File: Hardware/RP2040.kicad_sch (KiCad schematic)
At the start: 29 parts, among them J1 USB_B, SW2 SW_Push_Dual, U1 W25Q128JVS, U2 RP2040, Y1 ABM8-272-T3

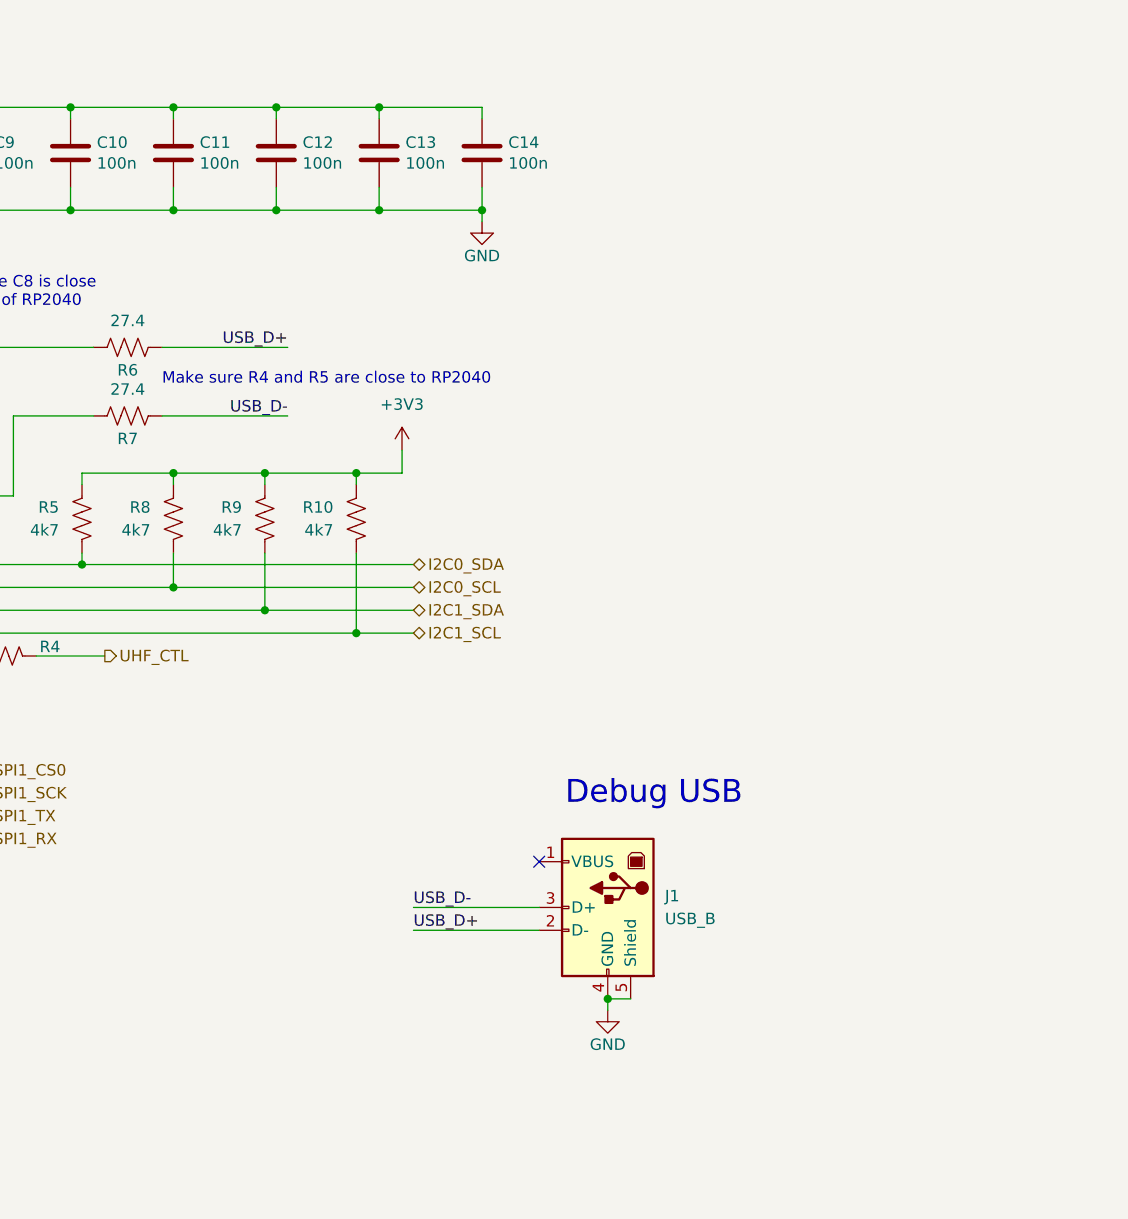
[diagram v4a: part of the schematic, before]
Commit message: Update USB connector to USBC
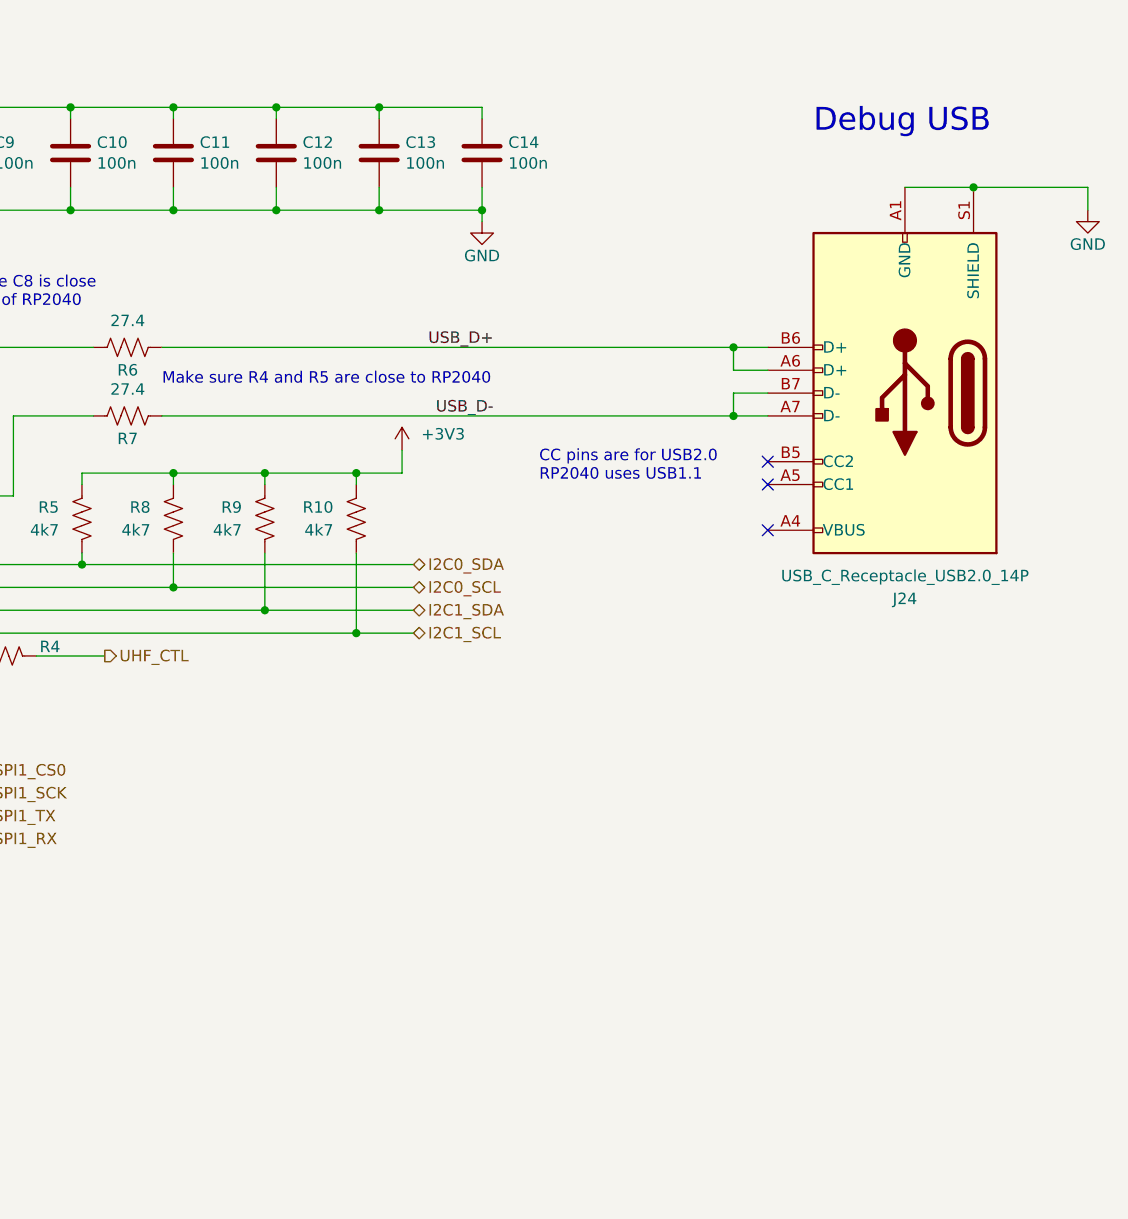
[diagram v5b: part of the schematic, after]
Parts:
- removed J1: USB_B, symbol Connector:USB_B
- added J24: USB_C_Receptacle_USB2.0_14P, symbol Connector:USB_C_Receptacle_USB2.0_14P
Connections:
- net GND: now also J24.A1 (GND), J24.A12 (GND), J24.B1 (GND), J24.B12 (GND), J24.S1 (SHIELD)
- net USB_D+: now also J24.A6 (D+), J24.B6 (D+)
- net USB_D-: now also J24.A7 (D-), J24.B7 (D-)
- new net: J24.A4 (VBUS), J24.A9 (VBUS), J24.B4 (VBUS), J24.B9 (VBUS)
- no-connect marks 1 -> 3
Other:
- note added: "CC pins are for USB2.0 RP2040 uses USB1.1"

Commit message: Update RP2040.kicad_sch
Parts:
- J24: footprint (none) -> Connector_USB:USB_C_Receptacle_JAE_DX07S024WJ3R400
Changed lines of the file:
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@@
 			)
 		)
-		(property "Footprint" ""
+		(property "Footprint" "Connector_USB:USB_C_Receptacle_JAE_DX07S024WJ3R400"
 			(at 344.17 93.98 0)
 			(effects

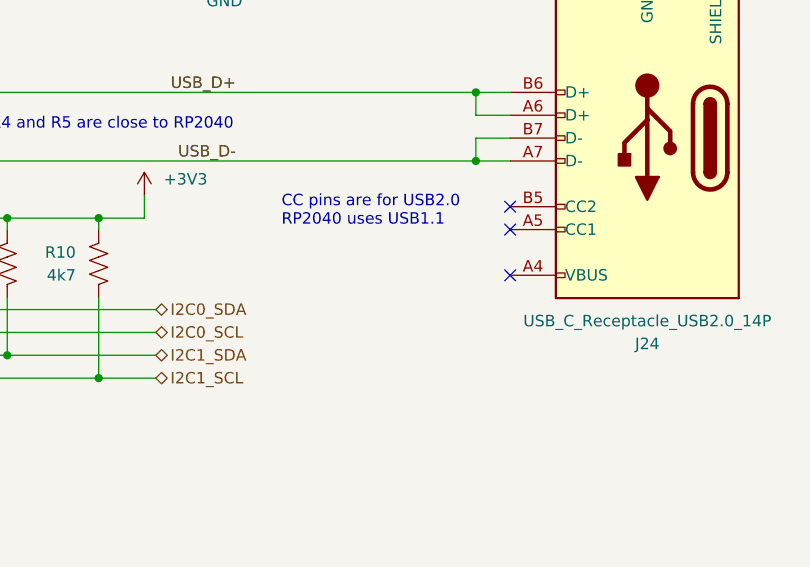
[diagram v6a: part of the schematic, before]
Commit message: Add USBC pull-downs
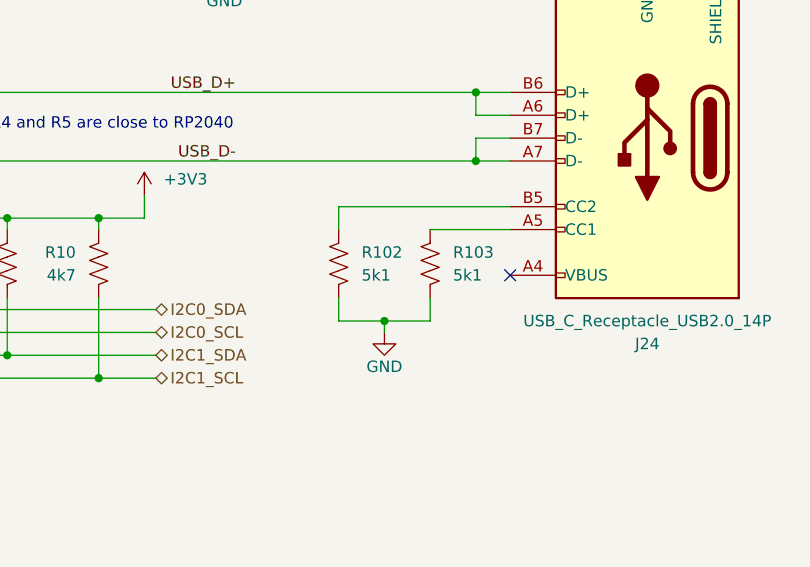
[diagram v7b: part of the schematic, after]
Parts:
- added R102, R103: 5k1, Resistor_SMD:R_0603_1608Metric, symbol Device:R_US
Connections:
- net GND: now also R102.2, R103.2
- net at J24.A5 (CC1): now also R103.1
- net at J24.B5 (CC2): now also R102.1
- no-connect marks 3 -> 1
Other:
- note removed: "CC pins are for USB2.0 RP2040 uses USB1.1"

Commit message: make most changes from design review
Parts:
- added R104, R108, R109, R110, R111, R112, R113: 22R, Resistor_SMD:R_0603_1608Metric, symbol Device:R_US
- added R105, R106, R107: 0R, Resistor_SMD:R_0603_1608Metric, symbol Device:R_US
- SW2: symbol Switch:SW_Push_Dual -> Switch:SW_Push
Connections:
- net GND: no longer SW2.4
- net SPI1_CS0: now also R107.1; no longer U2.12 (GPIO9)
- net SPI1_RX: now also R105.1; no longer U2.15 (GPIO12)
- net SPI1_SCK: now also R106.1; no longer U2.13 (GPIO10)
- net SPI1_TX: now also R104.1; no longer U2.14 (GPIO11)
- net UHF_CTL: now also R4.2; no longer R4.1
- net ~{BOOTSEL}: no longer SW2.3
- net at U2.51 (QSPI_SD3): now also R113.1; no longer U1.7 (IO3)
- net at U2.52 (QSPI_SCLK): now also R108.1; no longer U1.6 (CLK)
- net at U2.53 (QSPI_SD0): now also R110.1; no longer U1.5 (DI(IO0))
- net at U2.54 (QSPI_SD2): now also R112.1; no longer U1.3 (IO2)
- net at U2.55 (QSPI_SD1): now also R111.1; no longer U1.2 (DO(IO1))
- net at R2.1, U2.56 (QSPI_SS): now also R109.1; no longer R1.1, U1.1 (~{CS})
- net at U2.6 (GPIO4): now also R4.1; no longer R4.2
- new net: R107.2, U2.12 (GPIO9)
- new net: R106.2, U2.13 (GPIO10)
- new net: R104.2, U2.14 (GPIO11)
- new net: R105.2, U2.15 (GPIO12)
- new net: R111.2, U1.2 (DO(IO1))
- new net: R1.1, R109.2, U1.1 (~{CS})
- new net: R112.2, U1.3 (IO2)
- new net: R110.2, U1.5 (DI(IO0))
- new net: R113.2, U1.7 (IO3)
- new net RP2040_MEM_SCLK: R108.2, U1.6 (CLK)
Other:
- note added: "Flash should be close to the RP2040 due to shared impedance-matching resistors"
- moved on the sheet: R1, R4
